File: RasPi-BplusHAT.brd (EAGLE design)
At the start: 65 x 56 mm, 2 parts, among them K2 RASPI_HEADER

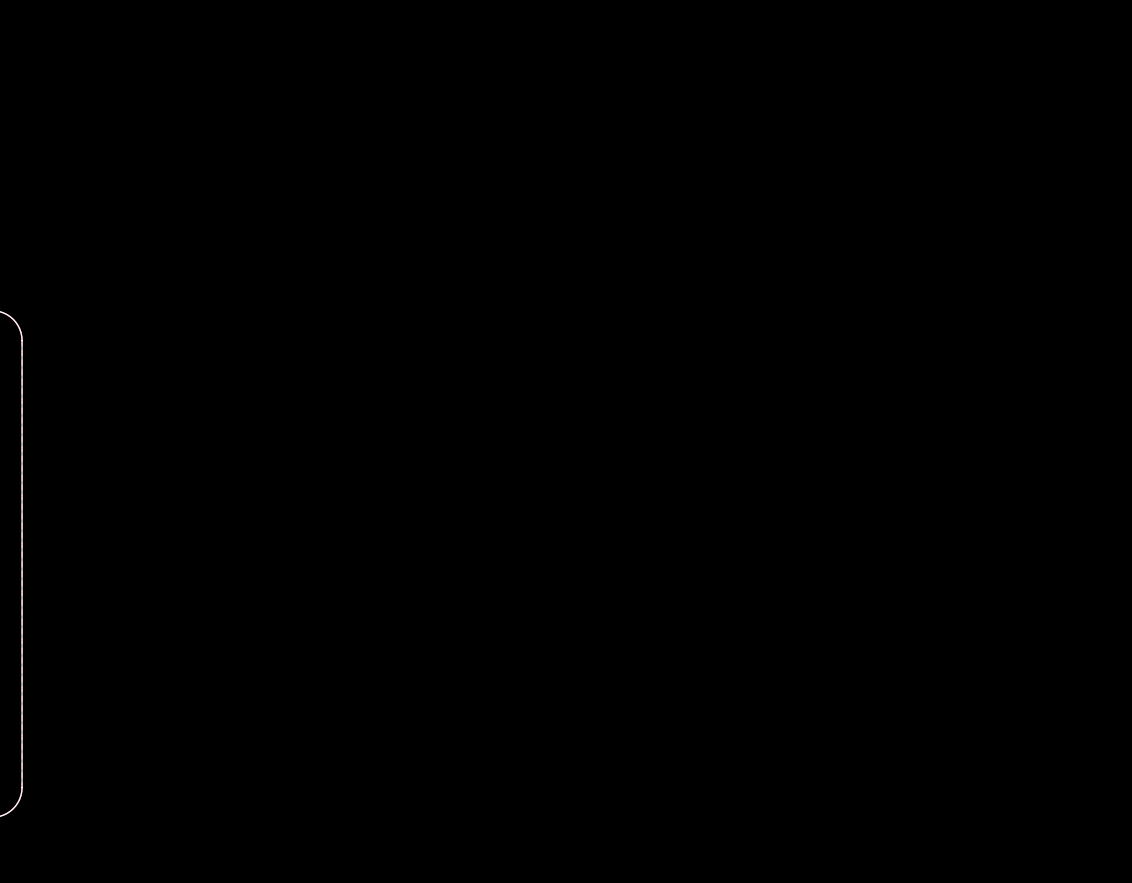
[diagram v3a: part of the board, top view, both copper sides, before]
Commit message: add pullups
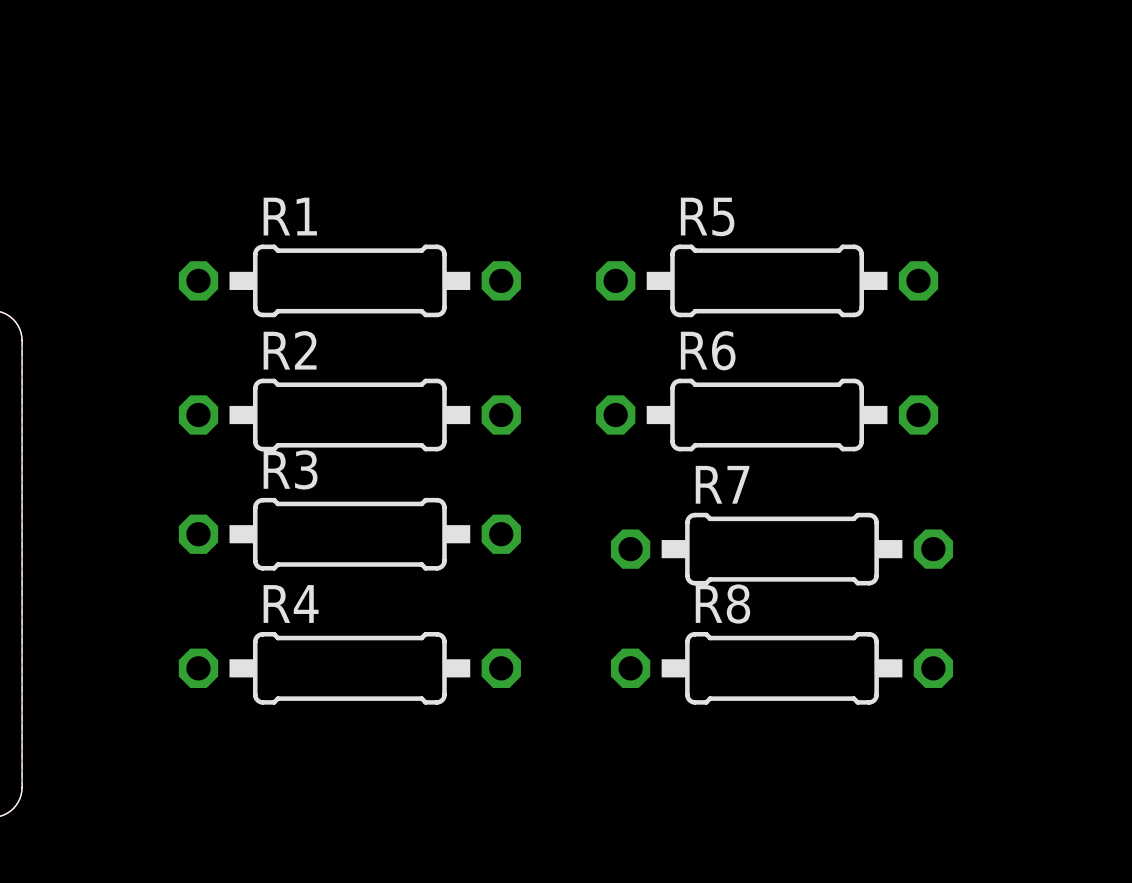
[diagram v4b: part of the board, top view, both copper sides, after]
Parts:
- added R1, R2, R3, R4, R5, R6, R7, R8: 10k, resistor:0207/10
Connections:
- net +3V3: now also R1.2, R2.2, R3.2, R4.2, R5.2, R6.2, R7.2, R8.2
- net DIGO18: now also R5.1
- net DIGO19: now also R6.1
- net DIGO20: now also R7.1
- net DIGO21: now also R8.1
- net DIGO5: now also R1.1
- net DIGO6: now also R2.1
- net DIGO7: now also R3.1
- net DIGO8: now also R4.1
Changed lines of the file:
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@@
 <layer number="97" name="Info" color="7" fill="1" visible="no" active="no"/>
 <layer number="98" name="Guide" color="6" fill="1" visible="no" active="no"/>
+<layer number="99" name="SpiceOrder" color="5" fill="1" visible="no" active="no"/>
 <layer number="100" name="NonViaHole" color="7" fill="1" visible="yes" active="yes"/>
 <layer number="101" name="PlacementGuide" color="7" fill="1" visible="yes" active="yes"/>
@@
 <attribute name="OC_FARNELL" value="unknown" x="32.5" y="10" size="1.778" layer="27" display="off"/>
 </element>
+<element name="R1" library="resistor" package="0207/10" value="10k" x="16" y="37.5"/>
+<element name="R2" library="resistor" package="0207/10" value="10k" x="16" y="33"/>
+<element name="R3" library="resistor" package="0207/10" value="10k" x="16" y="29"/>
+<element name="R4" library="resistor" package="0207/10" value="10k" x="16" y="24.5"/>
+<element name="R5" library="resistor" package="0207/10" value="10k" x="30" y="37.5"/>
+<element name="R6" library="resistor" package="0207/10" value="10k" x="30" y="33"/>
+<element name="R7" library="resistor" package="0207/10" value="10k" x="30.5" y="28.5"/>
+<element name="R8" library="resistor" package="0207/10" value="10k" x="30.5" y="24.5"/>
 </elements>
 <signals>
@@
 <contactref element="K2" pad="3V3"/>
 <contactref element="K2" pad="3.3V@17"/>
+<contactref element="R1" pad="2"/>
+<contactref element="R2" pad="2"/>
+<contactref element="R3" pad="2"/>
+<contactref element="R4" pad="2"/>
+<contactref element="R5" pad="2"/>
+<contactref element="R6" pad="2"/>
+<contactref element="R7" pad="2"/>
+<contactref element="R8" pad="2"/>
 <wire x1="8.37" y1="51.23" x2="28.69" y2="51.23" width="0" layer="19" extent="1-1"/>
+<wire x1="21.08" y1="37.5" x2="8.37" y2="51.23" width="0" layer="19" extent="1-1"/>
+<wire x1="21.08" y1="33" x2="21.08" y2="37.5" width="0" layer="19" extent="1-1"/>
+<wire x1="21.08" y1="29" x2="21.08" y2="33" width="0" layer="19" extent="1-1"/>
+<wire x1="21.08" y1="24.5" x2="21.08" y2="29" width="0" layer="19" extent="1-1"/>
+<wire x1="35.08" y1="37.5" x2="21.08" y2="24.5" width="0" layer="19" extent="1-1"/>
+<wire x1="35.08" y1="33" x2="35.08" y2="37.5" width="0" layer="19" extent="1-1"/>
+<wire x1="35.58" y1="28.5" x2="35.08" y2="33" width="0" layer="19" extent="1-1"/>
+<wire x1="35.58" y1="24.5" x2="35.58" y2="28.5" width="0" layer="19" extent="1-1"/>
 </signal>
 <signal name="+5V">
@@
 <signal name="DIGO5">
 <contactref element="X1" pad="5"/>
+<contactref element="R1" pad="1"/>
+<wire x1="10.92" y1="37.5" x2="26.9882" y2="11.27" width="0" layer="19" extent="1-1"/>
 </signal>
 <signal name="DIGO6">
 <contactref element="X1" pad="6"/>
+<contactref element="R2" pad="1"/>
+<wire x1="10.92" y1="33" x2="29.7314" y2="11.27" width="0" layer="19" extent="1-1"/>
 </signal>
 <signal name="DIGO7">
 <contactref element="X1" pad="7"/>
+<contactref element="R3" pad="1"/>
+<wire x1="10.92" y1="29" x2="32.5" y2="11.27" width="0" layer="19" extent="1-1"/>
 </signal>
 <signal name="DIGO8">
 <contactref element="X1" pad="8"/>
+<contactref element="R4" pad="1"/>
+<wire x1="10.92" y1="24.5" x2="35.2686" y2="11.27" width="0" layer="19" extent="1-1"/>
 </signal>
 <signal name="DIGIN9">
@@
 <signal name="DIGO18">
 <contactref element="X1" pad="18"/>
+<contactref element="R5" pad="1"/>
+<wire x1="24.92" y1="37.5" x2="28.3598" y2="8.73" width="0" layer="19" extent="1-1"/>
 </signal>
 <signal name="DIGO19">
 <contactref element="X1" pad="19"/>
+<contactref element="R6" pad="1"/>
+<wire x1="24.92" y1="33" x2="31.1284" y2="8.73" width="0" layer="19" extent="1-1"/>
 </signal>
 <signal name="DIGO20">
 <contactref element="X1" pad="20"/>
+<contactref element="R7" pad="1"/>
+<wire x1="25.42" y1="28.5" x2="33.8716" y2="8.73" width="0" layer="19" extent="1-1"/>
 </signal>
 <signal name="DIGO21">
 <contactref element="X1" pad="21"/>
+<contactref element="R8" pad="1"/>
+<wire x1="25.42" y1="24.5" x2="36.6402" y2="8.73" width="0" layer="19" extent="1-1"/>
 </signal>
 <signal name="DIGI22">

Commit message: hook up digo pins to gpios
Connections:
- net DIGO18: now also K2.GPIO12
- net DIGO19: now also K2.GPIO16
- net DIGO20: now also K2.GPIO20
- net DIGO21: now also K2.GPIO21
- net DIGO5: now also K2.GPIO18
- net DIGO6: now also K2.GPIO23
- net DIGO7: now also K2.GPIO24
- net DIGO8: now also K2.GPIO25
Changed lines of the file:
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@@
 <contactref element="X1" pad="5"/>
 <contactref element="R1" pad="1"/>
-<wire x1="10.92" y1="37.5" x2="26.9882" y2="11.27" width="0" layer="19" extent="1-1"/>
+<contactref element="K2" pad="GPIO18"/>
+<wire x1="10.92" y1="37.5" x2="21.07" y2="53.77" width="0" layer="19" extent="1-1"/>
+<wire x1="26.9882" y1="11.27" x2="10.92" y2="37.5" width="0" layer="19" extent="1-1"/>
 </signal>
 <signal name="DIGO6">
 <contactref element="X1" pad="6"/>
 <contactref element="R2" pad="1"/>
-<wire x1="10.92" y1="33" x2="29.7314" y2="11.27" width="0" layer="19" extent="1-1"/>
+<contactref element="K2" pad="GPIO23"/>
+<wire x1="10.92" y1="33" x2="26.15" y2="53.77" width="0" layer="19" extent="1-1"/>
+<wire x1="29.7314" y1="11.27" x2="10.92" y2="33" width="0" layer="19" extent="1-1"/>
 </signal>
 <signal name="DIGO7">
 <contactref element="X1" pad="7"/>
 <contactref element="R3" pad="1"/>
-<wire x1="10.92" y1="29" x2="32.5" y2="11.27" width="0" layer="19" extent="1-1"/>
+<contactref element="K2" pad="GPIO24"/>
+<wire x1="10.92" y1="29" x2="28.69" y2="53.77" width="0" layer="19" extent="1-1"/>
+<wire x1="32.5" y1="11.27" x2="10.92" y2="29" width="0" layer="19" extent="1-1"/>
 </signal>
 <signal name="DIGO8">
 <contactref element="X1" pad="8"/>
 <contactref element="R4" pad="1"/>
-<wire x1="10.92" y1="24.5" x2="35.2686" y2="11.27" width="0" layer="19" extent="1-1"/>
+<contactref element="K2" pad="GPIO25"/>
+<wire x1="10.92" y1="24.5" x2="33.77" y2="53.77" width="0" layer="19" extent="1-1"/>
+<wire x1="35.2686" y1="11.27" x2="10.92" y2="24.5" width="0" layer="19" extent="1-1"/>
 </signal>
 <signal name="DIGIN9">
@@
 <contactref element="X1" pad="18"/>
 <contactref element="R5" pad="1"/>
-<wire x1="24.92" y1="37.5" x2="28.3598" y2="8.73" width="0" layer="19" extent="1-1"/>
+<contactref element="K2" pad="GPIO12"/>
+<wire x1="24.92" y1="37.5" x2="46.47" y2="53.77" width="0" layer="19" extent="1-1"/>
+<wire x1="28.3598" y1="8.73" x2="24.92" y2="37.5" width="0" layer="19" extent="1-1"/>
 </signal>
 <signal name="DIGO19">
 <contactref element="X1" pad="19"/>
 <contactref element="R6" pad="1"/>
-<wire x1="24.92" y1="33" x2="31.1284" y2="8.73" width="0" layer="19" extent="1-1"/>
+<contactref element="K2" pad="GPIO16"/>
+<wire x1="24.92" y1="33" x2="51.55" y2="53.77" width="0" layer="19" extent="1-1"/>
+<wire x1="31.1284" y1="8.73" x2="24.92" y2="33" width="0" layer="19" extent="1-1"/>
 </signal>
 <signal name="DIGO20">
 <contactref element="X1" pad="20"/>
 <contactref element="R7" pad="1"/>
-<wire x1="25.42" y1="28.5" x2="33.8716" y2="8.73" width="0" layer="19" extent="1-1"/>
+<contactref element="K2" pad="GPIO20"/>
+<wire x1="25.42" y1="28.5" x2="54.09" y2="53.77" width="0" layer="19" extent="1-1"/>
+<wire x1="33.8716" y1="8.73" x2="25.42" y2="28.5" width="0" layer="19" extent="1-1"/>
 </signal>
 <signal name="DIGO21">
 <contactref element="X1" pad="21"/>
 <contactref element="R8" pad="1"/>
-<wire x1="25.42" y1="24.5" x2="36.6402" y2="8.73" width="0" layer="19" extent="1-1"/>
+<contactref element="K2" pad="GPIO21"/>
+<wire x1="25.42" y1="24.5" x2="56.63" y2="53.77" width="0" layer="19" extent="1-1"/>
+<wire x1="36.6402" y1="8.73" x2="25.42" y2="24.5" width="0" layer="19" extent="1-1"/>
 </signal>
 <signal name="DIGI22">

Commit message: route
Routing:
- net +3V3: track 0.00 -> 77.2 mm
- net DIGO8: track 0.00 -> 68.8 mm
- net DIGO7: track 0.00 -> 66.0 mm
- net DIGO21: track 0.00 -> 65.2 mm
- net DIGO19: track 0.00 -> 64.2 mm
- net DIGO20: track 0.00 -> 64.2 mm
- net DIGO18: track 0.00 -> 63.4 mm
- net DIGO6: track 0.00 -> 56.8 mm
- net DIGO5: track 0.00 -> 55.8 mm
- net +5V: track 0.00 -> 2.56 mm
